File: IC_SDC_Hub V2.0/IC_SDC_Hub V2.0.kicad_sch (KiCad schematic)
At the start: 12 parts, among them J1 Conn_01x02, J2 Conn_01x02, J3 Conn_01x02, J4 Conn_01x02, J5 Conn_01x02, J6 Conn_01x02, J7 Conn_01x04, J8 Conn_01x02, J9 Conn_01x02, Q1 BSS205N

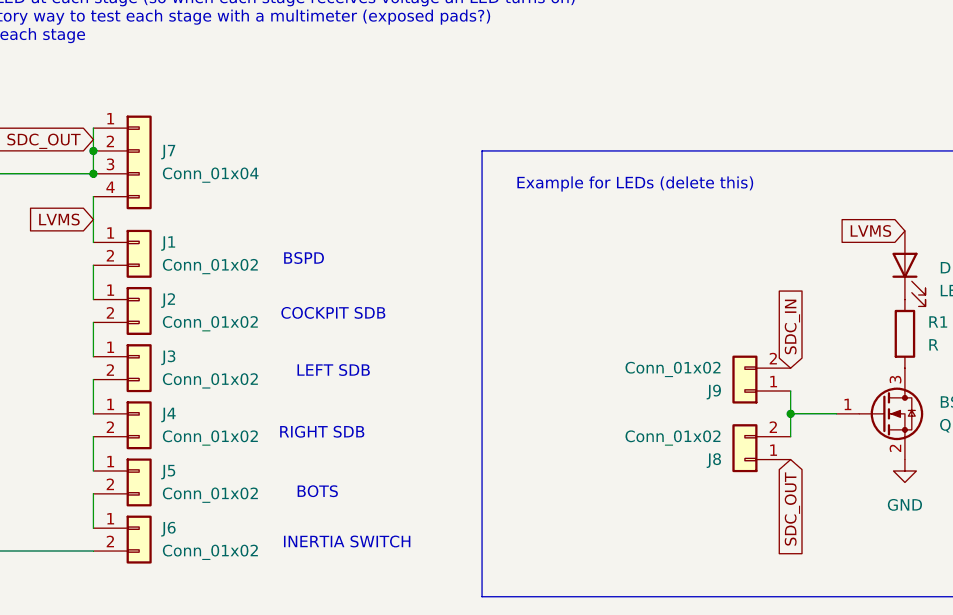
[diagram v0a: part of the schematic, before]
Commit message: Updated to match connector spec
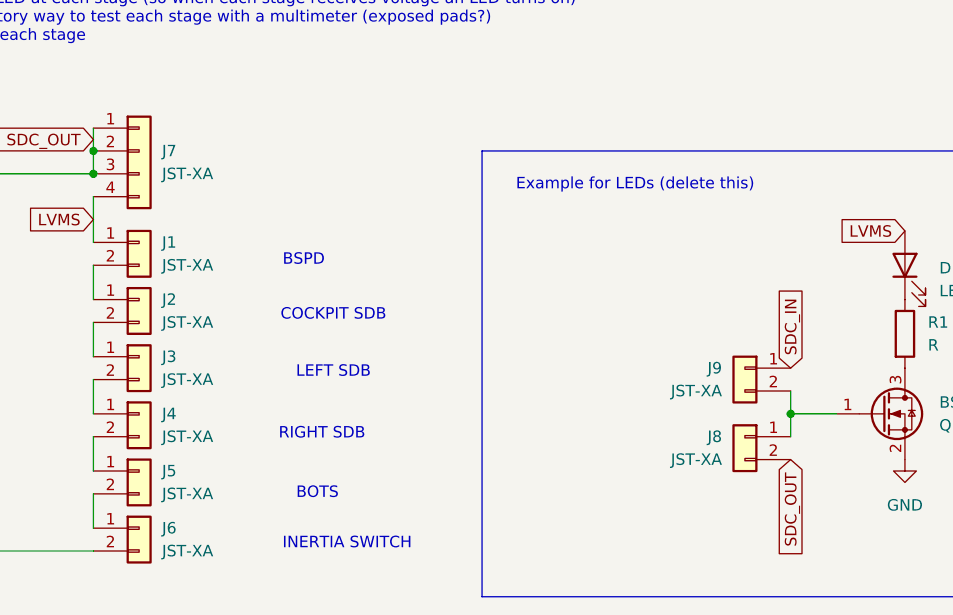
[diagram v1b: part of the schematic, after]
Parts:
- removed J1, J2, J3, J4, J5, J6, J8, J9: Conn_01x02, symbol Connector_Generic:Conn_01x02
- removed J7: Conn_01x04, symbol Connector_Generic:Conn_01x04
- added J1, J2, J3, J4, J5, J6, J8, J9: JST-XA, Custom_MSM:Connector_JST-XA_2POS, symbol Custom_MSM:Connector_JST-XA_2POS
- added J7: JST-XA, Custom_MSM:Connector_JST-XA_4POS, symbol Custom_MSM:Connector_JST-XA_4POS
- Q1, R1: now left out of the parts list
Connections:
- net LVMS: now also J1.1 (Pin_1), J7.4 (Pin_4)
- net SDC_IN: now also J9.1 (Pin_1)
- net SDC_OUT: now also J6.2 (Pin_2), J7.1 (Pin_1), J7.2 (Pin_2), J7.3 (Pin_3), J8.2 (Pin_2)
- net at Q1.1 (G): now also J8.1 (Pin_1), J9.2 (Pin_2)
- new net: J5.2 (Pin_2), J6.1 (Pin_1)
- new net: J3.2 (Pin_2), J4.1 (Pin_1)
- new net: J4.2 (Pin_2), J5.1 (Pin_1)
- new net: J1.2 (Pin_2), J2.1 (Pin_1)
- new net: J2.2 (Pin_2), J3.1 (Pin_1)

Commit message: Add files via upload
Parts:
- removed D1: LED, symbol Device:LED
- removed J8, J9: JST-XA, Custom_MSM:Connector_JST-XA_2POS, symbol Custom_MSM:Connector_JST-XA_2POS
- removed Q1: BSS205N, Custom_MSM:MOSFET_Single_SOT-23, symbol Custom_MSM:MOSFET_N-CH
- removed R1: R, symbol Device:R
- added D2, D3, D4, D5, D6, D7: LED, symbol Device:LED
- added Q2, Q3, Q4, Q5, Q6, Q7: BSS205N, Custom_MSM:MOSFET_Single_SOT-23, symbol Custom_MSM:MOSFET_N-CH
- added R2, R3, R4, R5, R6, R7: R, symbol Device:R
- added TP1, TP2, TP3, TP4, TP5, TP6: TestPoint, symbol Connector:TestPoint
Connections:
- net GND: now also Q2.2 (S), Q3.2 (S), Q4.2 (S), Q5.2 (S), Q6.2 (S), Q7.2 (S)
- net LVMS: now also D2.2 (A), D3.2 (A), D4.2 (A), D5.2 (A), D6.2 (A), D7.2 (A)
- net SDC_OUT: now also Q7.1 (G)
- net at J5.2 (Pin_2), J6.1 (Pin_1): now also Q6.1 (G)
- net at J3.2 (Pin_2), J4.1 (Pin_1): now also Q4.1 (G)
- net at J4.2 (Pin_2), J5.1 (Pin_1): now also Q5.1 (G)
- net at J1.2 (Pin_2), J2.1 (Pin_1): now also Q2.1 (G)
- net at J2.2 (Pin_2), J3.1 (Pin_1): now also Q3.1 (G)
- new net: Q2.3 (D), R2.2, TP6.1
- new net: D5.1 (K), R5.1
- new net: Q3.3 (D), R3.2, TP5.1
- new net: Q7.3 (D), R7.2, TP1.1
- new net: D3.1 (K), R3.1
- new net: D2.1 (K), R2.1
- new net: D6.1 (K), R6.1
- new net: Q6.3 (D), R6.2, TP2.1
- new net: Q4.3 (D), R4.2, TP4.1
- new net: D7.1 (K), R7.1
- new net: D4.1 (K), R4.1
- new net: Q5.3 (D), R5.2, TP3.1
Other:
- note removed: "Example for LEDs (delete this)"

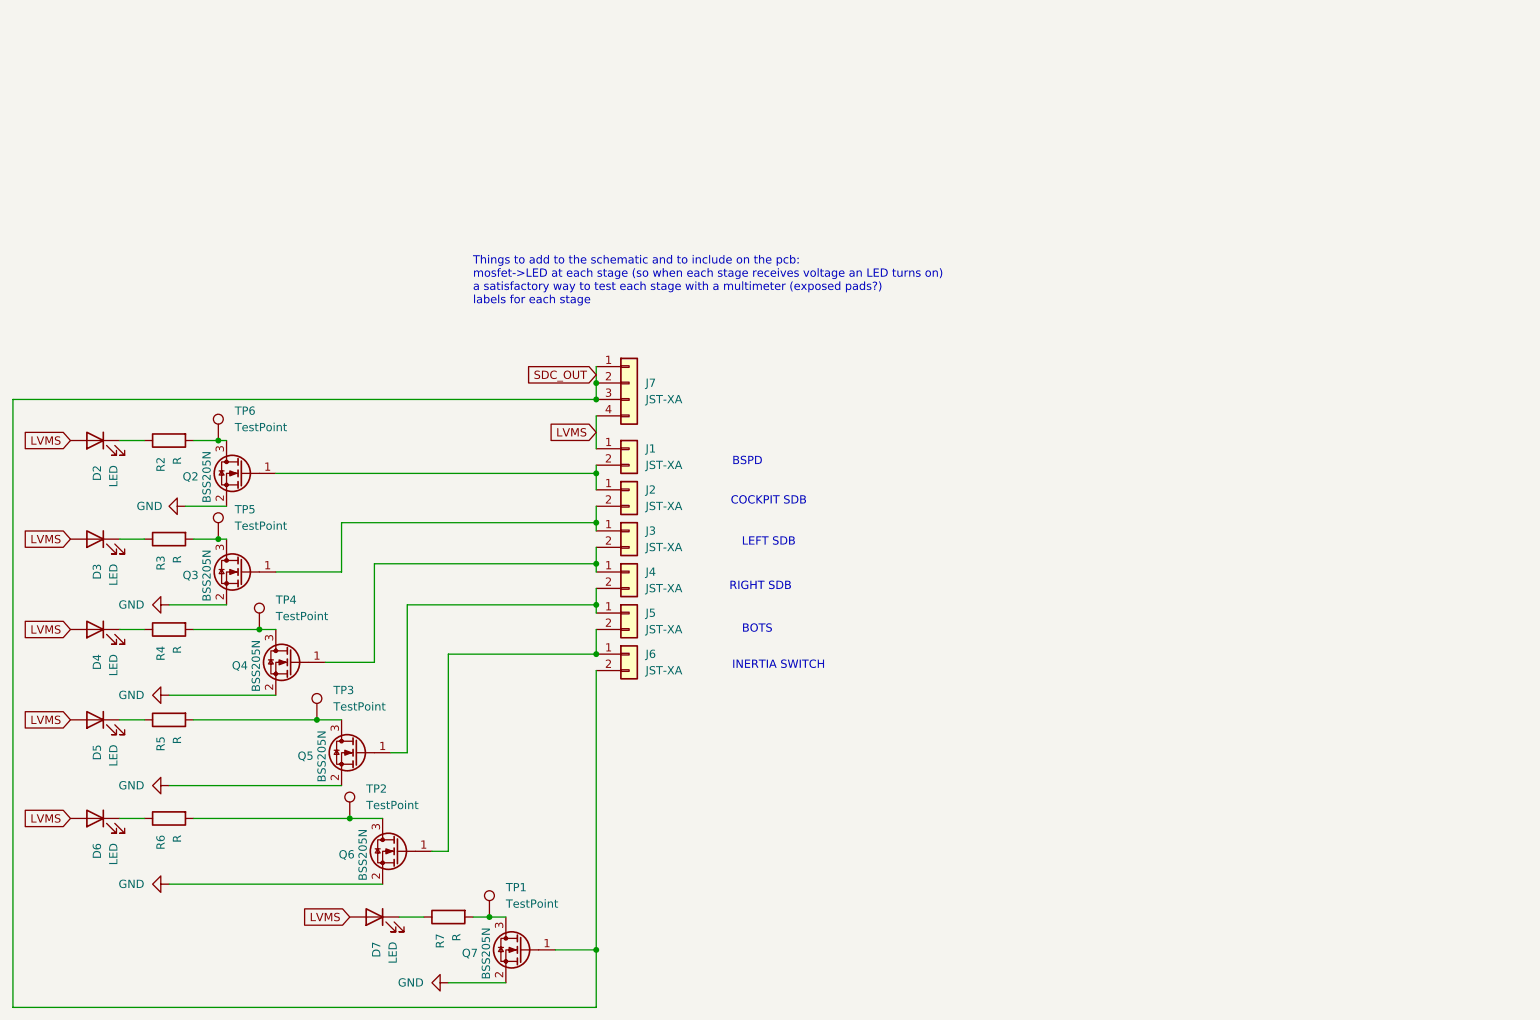
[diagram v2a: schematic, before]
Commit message: Add SDC Status Connectors
to be compatiable with new PDM
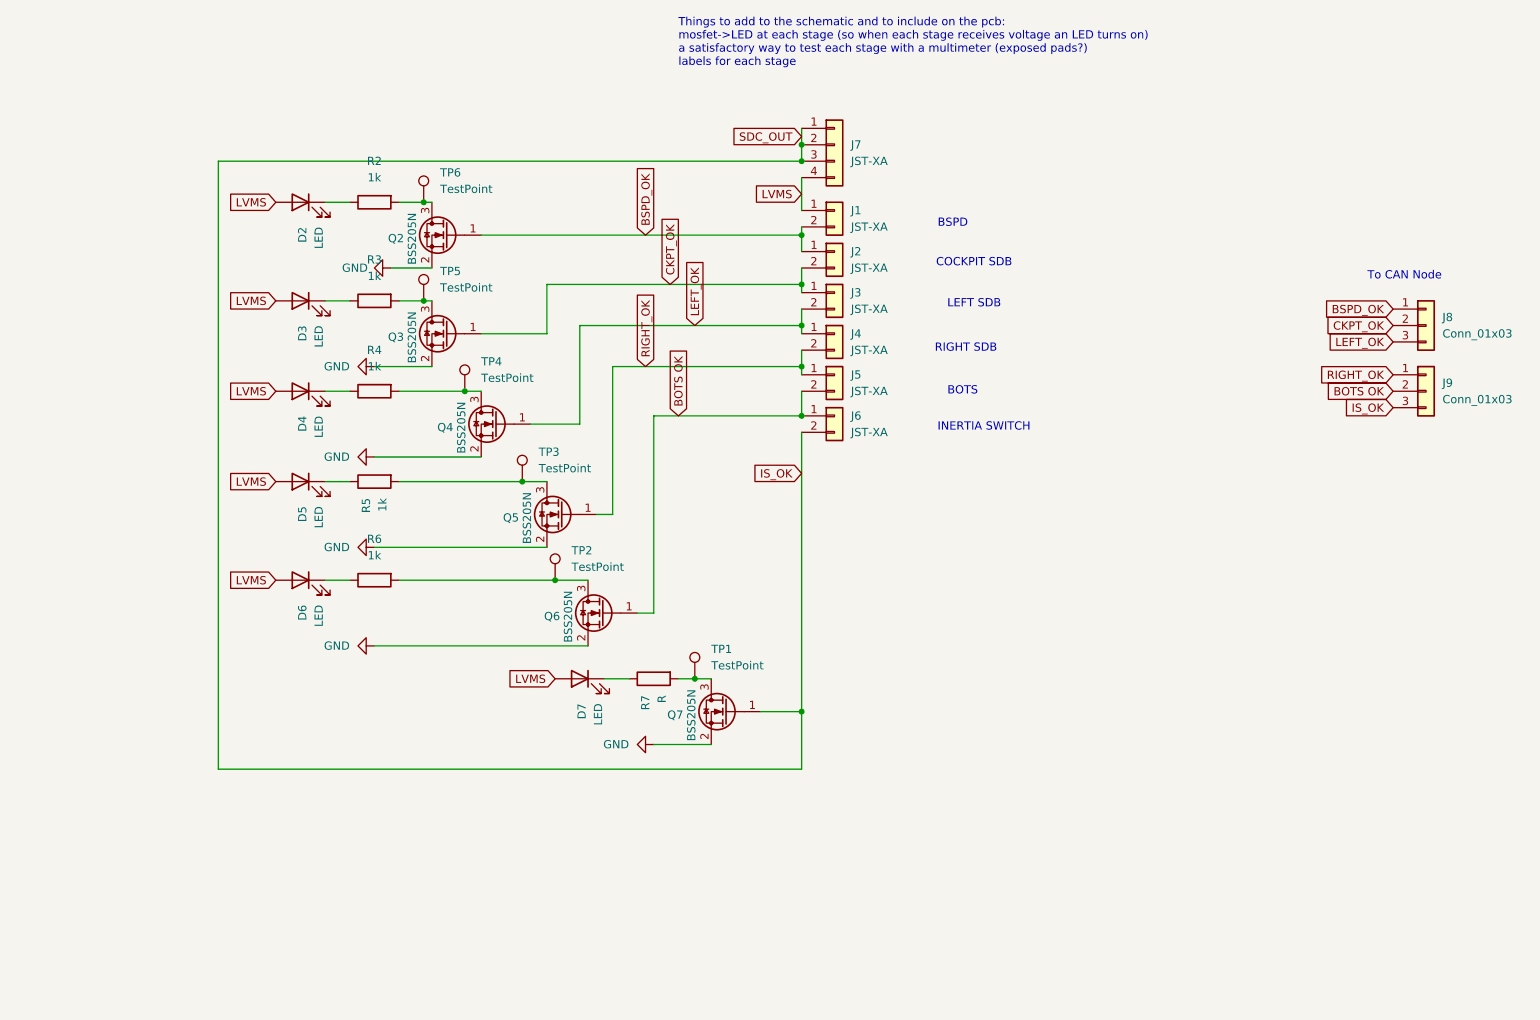
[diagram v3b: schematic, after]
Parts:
- added J8, J9: Conn_01x03, symbol Connector_Generic:Conn_01x03
- R2, R3, R4, R5, R6: value R -> 1k
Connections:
- net BOTS OK: now reaches J5.2 (Pin_2), J6.1 (Pin_1), Q6.1 (G)
- net BOTS OK: now also J9.2 (Pin_2)
- net LEFT_OK: now reaches J3.2 (Pin_2), J4.1 (Pin_1), Q4.1 (G)
- net LEFT_OK: now also J8.3 (Pin_3)
- net RIGHT_OK: now reaches J4.2 (Pin_2), J5.1 (Pin_1), Q5.1 (G)
- net RIGHT_OK: now also J9.1 (Pin_1)
- net BSPD_OK: now reaches J1.2 (Pin_2), J2.1 (Pin_1), Q2.1 (G)
- net BSPD_OK: now also J8.1 (Pin_1)
- net CKPT_OK: now reaches J2.2 (Pin_2), J3.1 (Pin_1), Q3.1 (G)
- net CKPT_OK: now also J8.2 (Pin_2)
- net SDC_OUT renamed IS_OK
- net IS_OK: now also J9.3 (Pin_3)
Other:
- note added: "To CAN Node"
- moved on the sheet: D2, D3, D4, D5, D6, D7, J1, J2, J3, J4, J5, J6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

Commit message: Add files via upload
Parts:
- removed Q7: BSS205N, Custom_MSM:MOSFET_Single_SOT-23, symbol Custom_MSM:MOSFET_N-CH
- added Q1: BSS205N, Custom_MSM:MOSFET_Single_SOT-23, symbol Custom_MSM:MOSFET_N-CH
- D2, D3, D4, D5, D6, D7: footprint (none) -> LED_SMD:LED_0201_0603Metric
- J8, J9: footprint (none) -> Connector_JST:JST_XA_S03B-XASK-1_1x03_P2.50mm_Horizontal
- Q2, Q3, Q4, Q5, Q6: now in the parts list
- R7: value R -> 1k
- TP1, TP2, TP3, TP4, TP5, TP6: footprint (none) -> Capacitor_SMD:C_0201_0603Metric_Pad0.64x0.40mm_HandSolder
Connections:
- net BOTS OK: now also Q2.1 (G); no longer Q6.1 (G)
- net BSPD_OK: now also Q6.1 (G); no longer Q2.1 (G)
- net CKPT_OK: now also Q5.1 (G); no longer Q3.1 (G)
- net GND: now also Q1.2 (S)
- net IS_OK: now also Q1.1 (G)
- net RIGHT_OK: now also Q3.1 (G); no longer Q5.1 (G)
- net at R2.2, TP6.1: now also Q6.3 (D); no longer Q2.3 (D)
- net at R3.2, TP5.1: now also Q5.3 (D); no longer Q3.3 (D)
- net at R7.2, TP1.1: now also Q1.3 (D)
- net at R6.2, TP2.1: now also Q2.3 (D); no longer Q6.3 (D)
- net at R5.2, TP3.1: now also Q3.3 (D); no longer Q5.3 (D)
